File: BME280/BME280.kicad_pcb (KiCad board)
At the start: 2 copper layers, 17.8 x 14.4 mm, 21 parts, among them J1 Conn_01x07, Q1 BSS138DW, Q2 BSS138DW, U1 AP2127K-3.3

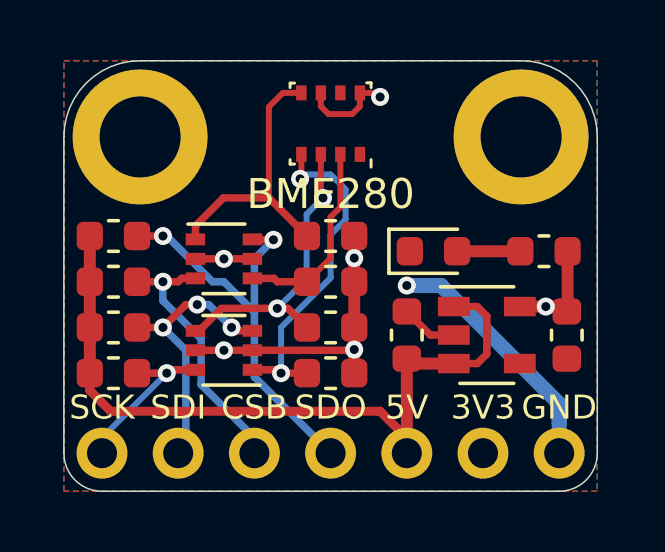
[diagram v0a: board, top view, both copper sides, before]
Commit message: BME280 Part number edits
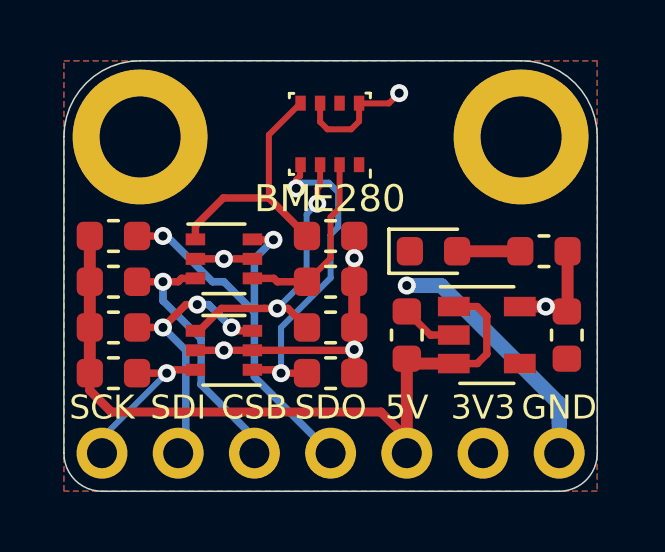
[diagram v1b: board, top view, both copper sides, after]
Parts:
- moved BME280 0.34 mm to (63.3, 29.4)
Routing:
- net 3V3: track 18.6 -> 19.7 mm
- net SDO_3V3: track 9.43 -> 8.72 mm
